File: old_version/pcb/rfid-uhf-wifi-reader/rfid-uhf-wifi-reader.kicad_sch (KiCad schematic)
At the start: 23 parts, among them J1 USB_OTG, J2 Conn_01x05, Q1 BSS138, Q2 BSS138, SW1 SW_Push, SW2 SW_Push, U1 ESP32-WROOM-32, U2 AMS1117-3.3, U3 CH340E

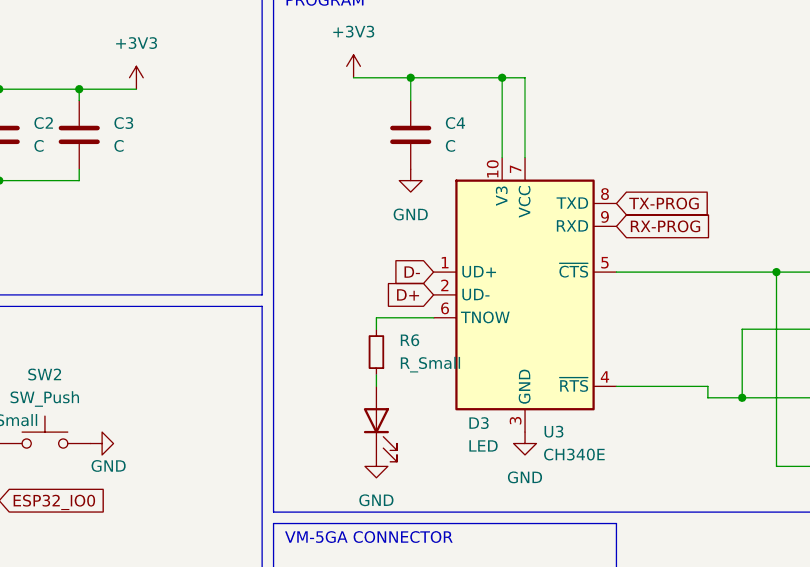
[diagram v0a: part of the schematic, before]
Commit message: fix usb data inverted
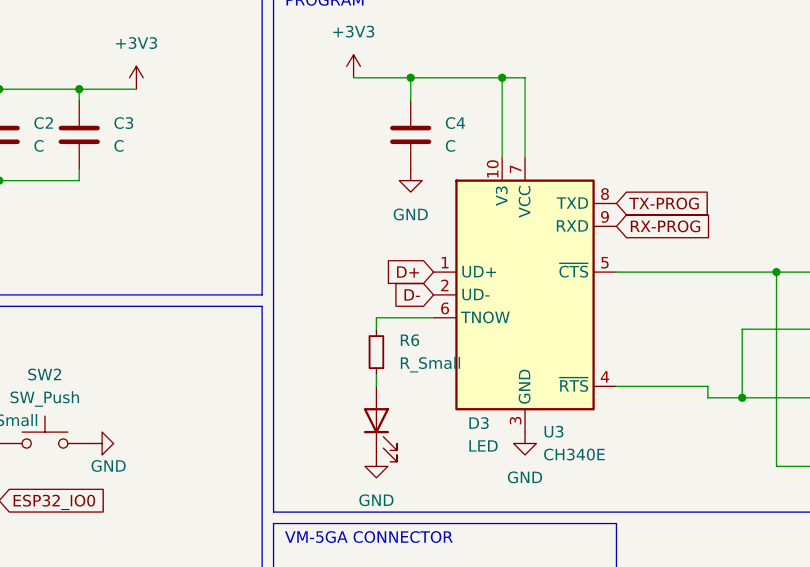
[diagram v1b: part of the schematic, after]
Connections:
- net D+: now also U3.1 (UD+); no longer U3.2 (UD-)
- net D-: now also U3.2 (UD-); no longer U3.1 (UD+)
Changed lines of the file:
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@@
+    )
+  )
+  (global_label "D+" (shape input) (at 129.54 45.72 180) (fields_autoplaced)
+    (effects (font (size 1.27 1.27)) (justify right))
+    (property "Intersheetrefs" "${INTERSHEET_REFS}" (at 124.2845 45.6406 0)
+      (effects (font (size 1.27 1.27)) (justify right) hide)
     )
   )
@@
     )
   )
-  (global_label "D-" (shape input) (at 129.54 45.72 180) (fields_autoplaced)
-    (effects (font (size 1.27 1.27)) (justify right))
-    (property "Intersheetrefs" "${INTERSHEET_REFS}" (at 124.2845 45.6406 0)
-      (effects (font (size 1.27 1.27)) (justify right) hide)
-    )
-  )
   (global_label "TX-PROG" (shape input) (at 64.77 78.74 0) (fields_autoplaced)
     (effects (font (size 1.27 1.27)) (justify left))
@@
     )
   )
-  (global_label "D+" (shape input) (at 129.54 48.26 180) (fields_autoplaced)
+  (global_label "D-" (shape input) (at 129.54 48.26 180) (fields_autoplaced)
     (effects (font (size 1.27 1.27)) (justify right))
     (property "Intersheetrefs" "${INTERSHEET_REFS}" (at 124.2845 48.1806 0)
